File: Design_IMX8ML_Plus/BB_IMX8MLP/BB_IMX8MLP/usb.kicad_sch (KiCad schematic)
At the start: 0 parts

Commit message: Add SPB228 WIFI/BLE module
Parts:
- added P2: USB_C_Plug, Connector_USB:USB_C_Receptacle_HRO_TYPE-C-31-M-12, symbol Connector:USB_C_Plug
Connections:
- new net: P2.A1 (GND), P2.A12 (GND), P2.B1 (GND), P2.B12 (GND)
- new net: P2.A4 (VBUS), P2.A9 (VBUS), P2.B4 (VBUS), P2.B9 (VBUS)
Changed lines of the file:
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@@
-(kicad_sch (version 20230121) (generator eeschema)
-  (paper "A4")
+(kicad_sch
+	(version 20231120)
+	(generator "eeschema")
+	(generator_version "8.0")
+	(paper "A4")
+	(symbol
+		(lib_id "Connector:USB_C_Plug")
+		(at 252.73 49.53 0)
+		(mirror y)
+		(unit 1)
+		(exclude_from_sim no)
+		(in_bom yes)
+		(on_board yes)
+		(dnp no)
+		(property "Reference" "P2"
+			(at 264.16 55.8801 0)
+			(effects
+				(font
+					(size 1.27 1.27)
+				)
+				(justify right)
+			)
+		)
+		(property "Value" "USB_C_Plug"
+			(at 264.16 53.3401 0)
+			(effects
+				(font
+					(size 1.27 1.27)
+				)
+				(justify right)
+			)
+		)
+		(property "Footprint" "Connector_USB:USB_C_Receptacle_HRO_TYPE-C-31-M-12"
+			(at 226.06 14.732 0)
+			(effects
+				(font
+					(size 1.27 1.27)
+				)
+				(justify right)
+			)
+		)
+		(property "Datasheet" "https://www.usb.org/sites/default/files/documents/usb_type-c.zip"
+			(at 248.92 49.53 0)
+			(effects
+				(font
+					(size 1.27 1.27)
+				)
+				(hide yes)
+			)
+		)
+		(property "Description" ""
+			(at 252.73 49.53 0)
+			(effects
+				(font
+					(size 1.27 1.27)
+				)
+				(hide yes)
+			)
+		)
+		(pin "A1"
+		)
+		(pin "A10"
+		)
+		(pin "A11"
+		)
+		(pin "A12"
+		)
+		(pin "A2"
+		)
+		(pin "A3"
+		)
+		(pin "A4"
+		)
+		(pin "A5"
+		)
+		(pin "A6"
+		)
+		(pin "A7"
+		)
+		(pin "A8"
+		)
+		(pin "A9"
+		)
+		(pin "B1"
+		)
+		(pin "B10"
+		)
+		(pin "B11"
+		)
+		(pin "B12"
+		)
+		(pin "B2"
+		)
+		(pin "B3"
+		)
+		(pin "B4"
+		)
+		(pin "B5"
+		)
+		(pin "B8"
+		)
+		(pin "B9"
+		)
+		(pin "S1"
+		)
+		(instances
+			(project "BB_IMX8MLP"
+				(path "/cd2fb234-91e5-476f-84ed-38419b628dc6/d45ee961-7c38-470c-a7ea-0552d843cfb4"
+					(reference "P2")
+					(unit 1)
+				)
+			)
+		)
+	)
 )

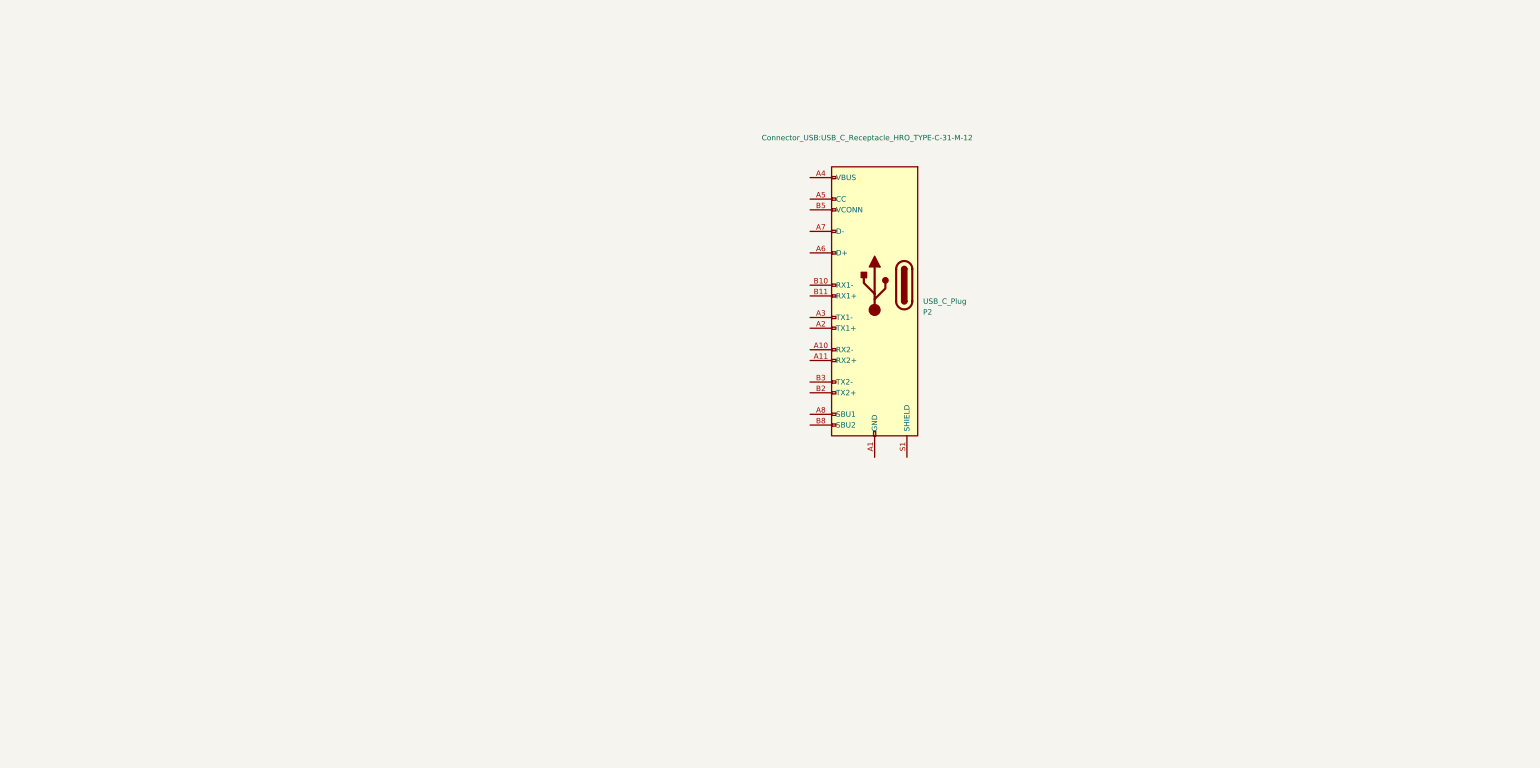
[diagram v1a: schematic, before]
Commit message: Improve power source module in the base board
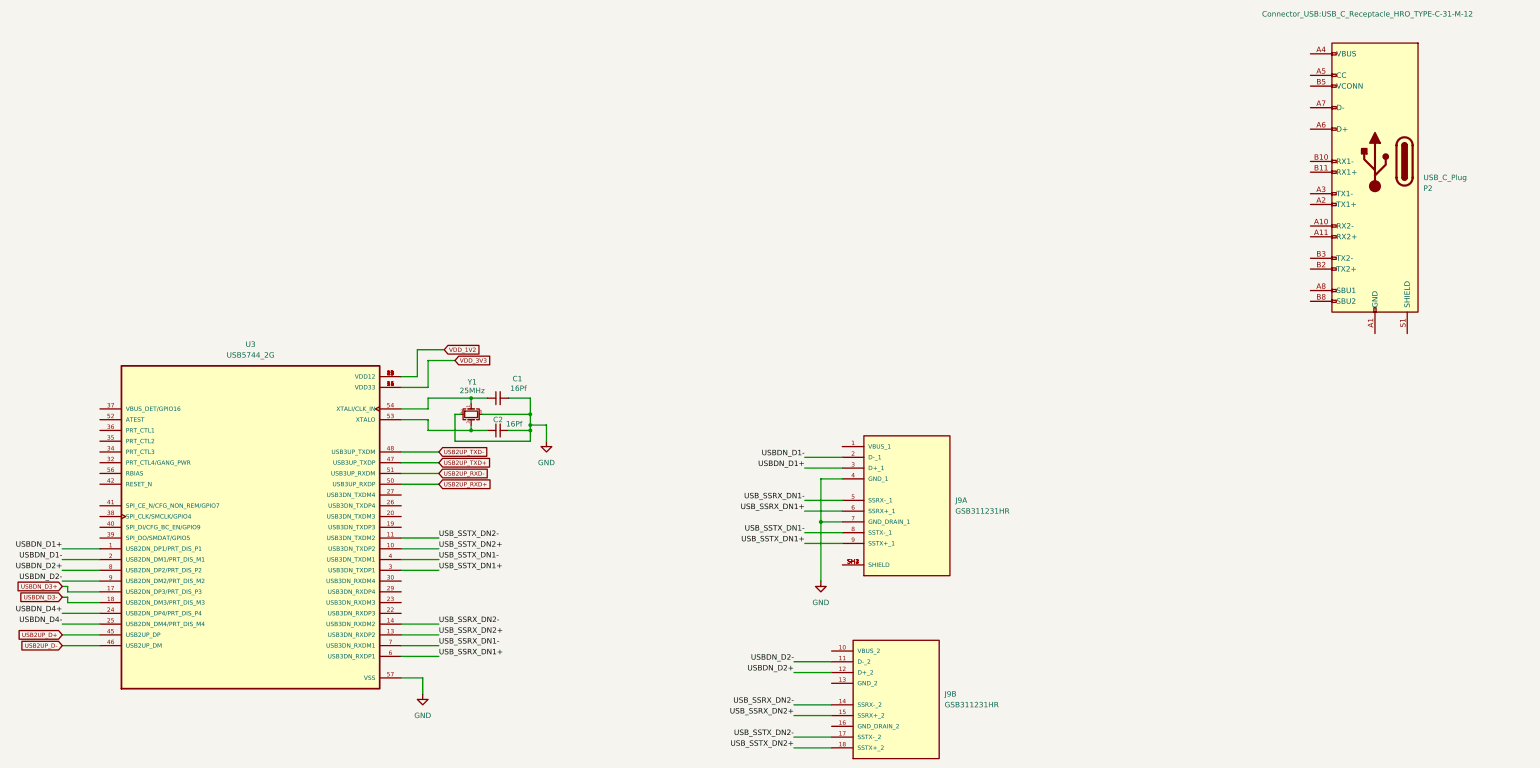
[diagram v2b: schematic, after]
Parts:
- added C1, C2: 16Pf, Capacitor_SMD:C_0402_1005Metric, symbol Device:C_Small
- added J9: GSB311231HR, _W_SBC:AMPHENOL_GSB311231HR, symbol GSB311231HR:GSB311231HR
- added U3: USB5744_2G, _W_SBC:QFN40P700X700X100-57N, symbol USB5744_2G:USB5744_2G
- added Y1: 25MHz, Crystal:Crystal_SMD_0603-4Pin_6.0x3.5mm, symbol Device:Crystal_GND24_Small
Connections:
- new net: C1.1, U3.54 (XTALI/CLK_IN), Y1.1
- new net: C2.1, U3.53 (XTALO), Y1.3
- new net: J9.SH1 (SHIELD), J9.SH2 (SHIELD), J9.SH3 (SHIELD), J9.SH4 (SHIELD)
- new net GND: C1.2, C2.2, J9.4 (GND_1), J9.7 (GND_DRAIN_1), U3.57 (VSS), Y1.2, Y1.4
- new net USB2UP_D+: U3.45 (USB2UP_DP)
- new net USB2UP_D-: U3.46 (USB2UP_DM)
- new net USB2UP_RXD+: U3.50 (USB3UP_RXDP)
- new net USB2UP_RXD-: U3.51 (USB3UP_RXDM)
- new net USB2UP_TXD+: U3.47 (USB3UP_TXDP)
- new net USB2UP_TXD-: U3.48 (USB3UP_TXDM)
- new net USBDN_D1+: J9.3 (D+_1), U3.1 (USB2DN_DP1/PRT_DIS_P1)
- new net USBDN_D1-: J9.2 (D-_1), U3.2 (USB2DN_DM1/PRT_DIS_M1)
- new net USBDN_D2+: J9.12 (D+_2), U3.8 (USB2DN_DP2/PRT_DIS_P2)
- new net USBDN_D2-: J9.11 (D-_2), U3.9 (USB2DN_DM2/PRT_DIS_M2)
- new net USBDN_D3+: U3.17 (USB2DN_DP3/PRT_DIS_P3)
- new net USBDN_D3-: U3.18 (USB2DN_DM3/PRT_DIS_M3)
- new net USBDN_D4+: U3.24 (USB2DN_DP4/PRT_DIS_P4)
- new net USBDN_D4-: U3.25 (USB2DN_DM4/PRT_DIS_M4)
- new net USB_SSRX_DN1+: J9.6 (SSRX+_1), U3.6 (USB3DN_RXDP1)
- new net USB_SSRX_DN1-: J9.5 (SSRX-_1), U3.7 (USB3DN_RXDM1)
- new net USB_SSRX_DN2+: J9.15 (SSRX+_2), U3.13 (USB3DN_RXDP2)
- new net USB_SSRX_DN2-: J9.14 (SSRX-_2), U3.14 (USB3DN_RXDM2)
- new net USB_SSTX_DN1+: J9.9 (SSTX+_1), U3.3 (USB3DN_TXDP1)
- new net USB_SSTX_DN1-: J9.8 (SSTX-_1), U3.4 (USB3DN_TXDM1)
- new net USB_SSTX_DN2+: J9.18 (SSTX+_2), U3.10 (USB3DN_TXDP2)
- new net USB_SSTX_DN2-: J9.17 (SSTX-_2), U3.11 (USB3DN_TXDM2)
- new net VDD_1V2: U3.12 (VDD12), U3.15 (VDD12), U3.21 (VDD12), U3.28 (VDD12), U3.33 (VDD12), U3.43 (VDD12), U3.49 (VDD12), U3.5 (VDD12)
- new net VDD_3V3: U3.16 (VDD33), U3.31 (VDD33), U3.44 (VDD33), U3.55 (VDD33)
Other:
- moved on the sheet: P2

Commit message: improving the usb conector
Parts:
- removed J9: GSB311231HR, _W_SBC:AMPHENOL_GSB311231HR, symbol GSB311231HR:GSB311231HR
- removed P2: USB_C_Plug, Connector_USB:USB_C_Receptacle_HRO_TYPE-C-31-M-12, symbol Connector:USB_C_Plug
- added C29: 10uF, Capacitor_SMD:C_0402_1005Metric, symbol Device:C_Small
- added C30, C31, C32, C33, C34, C35, C36, C37, C41, C42, C43, C44: 100nF, Capacitor_SMD:C_0402_1005Metric, symbol Device:C_Small
- added C38, C39, C45, C46: 1nF, Capacitor_SMD:C_0402_1005Metric, symbol Device:C_Small
- added C40: 4.7uF, Capacitor_SMD:C_0402_1005Metric, symbol Device:C_Small
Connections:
- net GND: now also C29.2, C30.2, C31.2, C32.2, C33.2, C34.2, C35.2, C36.2, C37.2, C38.2, C39.2, C40.2, C41.2, C42.2, C43.2, C44.2, C45.2, C46.2
- net VDD_1V2: now also C29.1, C30.1, C31.1, C32.1, C33.1, C34.1, C35.1, C36.1, C37.1, C38.1, C39.1
- net VDD_3V3: now also C40.1, C41.1, C42.1, C43.1, C44.1, C45.1, C46.1
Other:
- added sheet usb_connectors (usb_connectors.kicad_sch)

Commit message: improving Ethernet, USB and Camera inteface
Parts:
- added C73, C74: 100nF, Capacitor_SMD:C_0402_1005Metric, symbol Device:C_Small
- added U16: ~, _W_SBC:MICROPAK8_1P6X1P6_ONS, symbol _W_MX8M:FXMA2102L8X
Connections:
- net GND: now also C73.2, C74.2, U16.4 (GND)
- net USBH3_SSTX+: now reaches U3.19 (USB3DN_TXDP3)
- net USBH3_SSTX-: now reaches U3.20 (USB3DN_TXDM3)
- net USBH3_SSRX+: now reaches U3.22 (USB3DN_RXDP3)
- net USBH3_SSRX-: now reaches U3.23 (USB3DN_RXDM3)
- net USBH3_PRT_CTL: now reaches U3.34 (PRT_CTL3)
- net USBH2_PRT_CTL: now reaches U3.35 (PRT_CTL2)
- net USBDN_D1+: no longer names the net of U3.1 (USB2DN_DP1/PRT_DIS_P1)
- net USBDN_D1-: no longer names the net of U3.2 (USB2DN_DM1/PRT_DIS_M1)
- net USBDN_D2+ renamed USBH2_D+
- net USBDN_D2- renamed USBH2_D-
- net USBDN_D3+ renamed USBH3_D+
- net USBDN_D3- renamed USBH3_D-
- net USBDN_D4+ renamed USBH4_D+
- net USBDN_D4- renamed USBH4_D-
- net USB_SSRX_DN1+: no longer names the net of U3.6 (USB3DN_RXDP1)
- net USB_SSRX_DN1-: no longer names the net of U3.7 (USB3DN_RXDM1)
- net USB_SSRX_DN2+ renamed USBH2_SSRX+
- net USB_SSRX_DN2- renamed USBH2_SSRX-
- net USB_SSTX_DN1+: no longer names the net of U3.3 (USB3DN_TXDP1)
- net USB_SSTX_DN1-: no longer names the net of U3.4 (USB3DN_TXDM1)
- net USB_SSTX_DN2+ renamed USBH2_SSTX+
- net USB_SSTX_DN2- renamed USBH2_SSTX-
- new net: C74.1, U16.8 (VCCB)
- new net: C73.1, U16.1 (VCCA)
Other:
- note added: "From Host"
- note added: "To_Connector"
- note added: "To_PCIe"

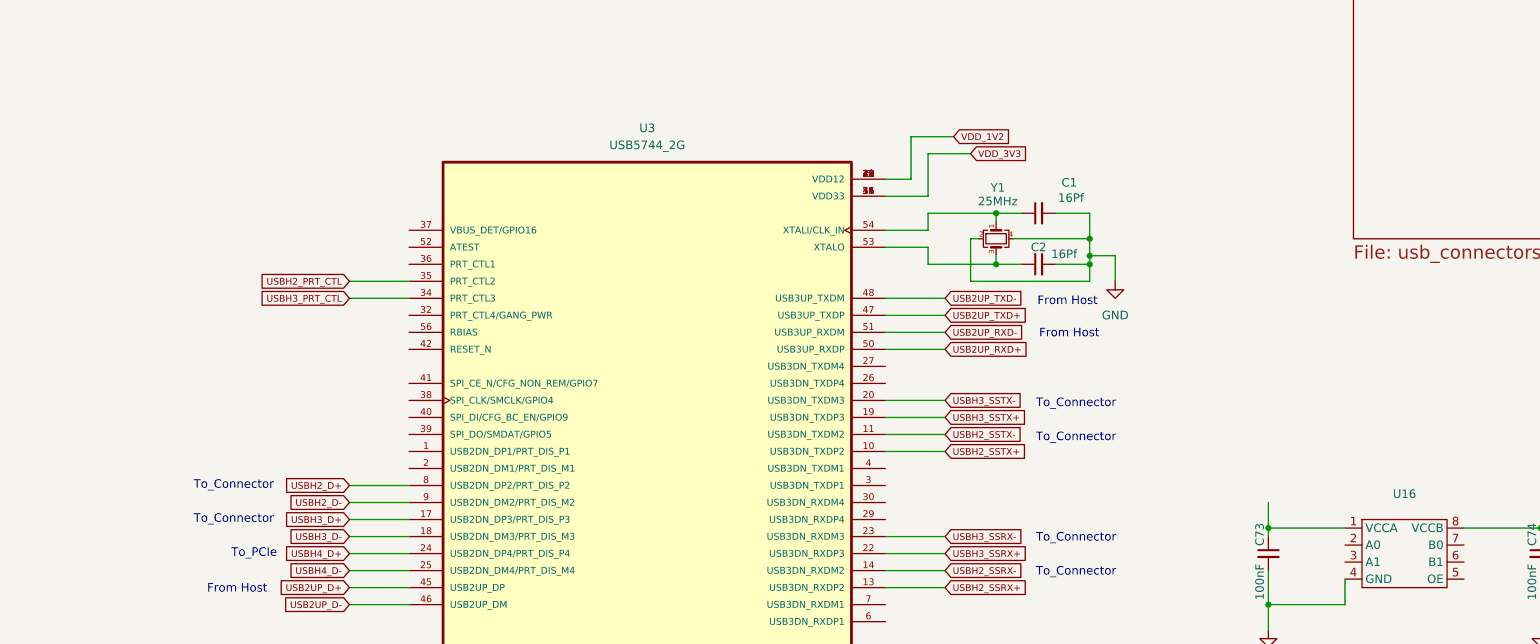
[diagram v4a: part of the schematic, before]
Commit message: Add LVDs and CSI Interface
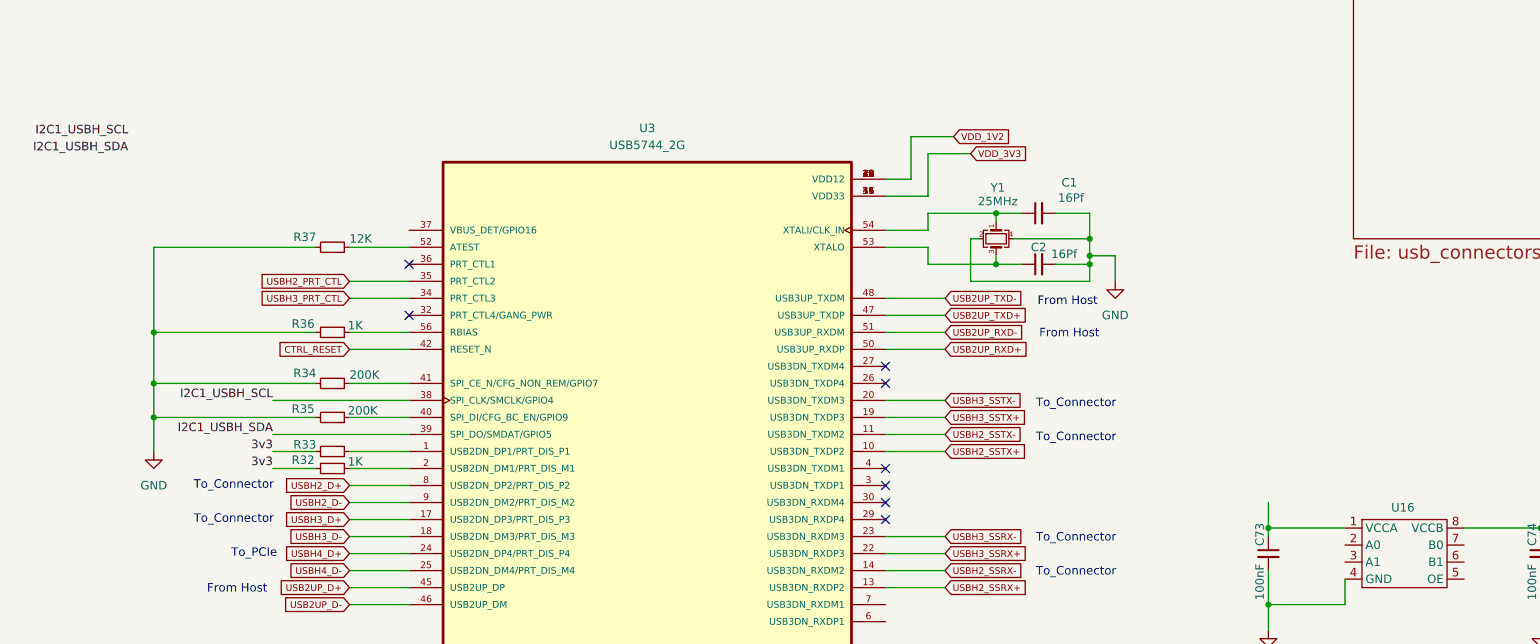
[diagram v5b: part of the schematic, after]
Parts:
- added R32, R33, R36: 1K, Resistor_SMD:R_0402_1005Metric, symbol Device:R_Small
- added R34, R35: 200K, Resistor_SMD:R_0402_1005Metric, symbol Device:R_Small
- added R37: 12K, Resistor_SMD:R_0402_1005Metric, symbol Device:R_Small
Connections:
- net GND: now also R34.2, R35.2, R36.2, R37.2
- net at U3.1 (USB2DN_DP1/PRT_DIS_P1): now also R33.1
- net at U3.2 (USB2DN_DM1/PRT_DIS_M1): now also R32.1
- net I2C1_USBH_SCL: now reaches U3.38 (SPI_CLK/SMCLK/GPIO4)
- net I2C1_USBH_SDA: now reaches U3.39 (SPI_DO/SMDAT/GPIO5)
- net at U3.40 (SPI_DI/CFG_BC_EN/GPIO9): now also R35.1
- net at U3.41 (SPI_CE_N/CFG_NON_REM/GPIO7): now also R34.1
- net CTRL_RESET: now reaches U3.42 (RESET_N)
- net at U3.52 (ATEST): now also R37.1
- net at U3.56 (RBIAS): now also R36.1
- new net 3v3: R32.2, R33.2
- no-connect marks 0 -> 8

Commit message: Review
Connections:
- net 3v3: now also C74.1, U16.8 (VCCB)
- net I2C1_USBH_SCL: now also U16.7 (B0)
- net I2C1_USBH_SDA: now also U16.6 (B1)
- net 1v8: now reaches C73.1, U16.1 (VCCA)
- net I2C1_SCL: now reaches U16.2 (A0)
- net I2C1_SDA: now reaches U16.3 (A1)
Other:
- moved on the sheet: C73, C74
